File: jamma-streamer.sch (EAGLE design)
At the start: 64 parts, among them IC1 LM7805, J1 Audio line out, J2 ICSP, J4 DM3AT-SF-PEJM5, J5 KMMX-BSMT35S-B30TR, T1 TY-145P, T2 TY-145P, U1 CD74HC165MD16-M, U10 LM358DTD8-M, U2 ATMEGA328PB-AUR, U3 74HC4050D, U4 TLV757X / LP298X, U5 CD74HC165MD16-M, U6 CD74HC165MD16-M, U7 FT232RL, U8 DS3231SNT&R21-0042B_16-M, U9 NDT2955SOT-223-M, Y1 16MHz

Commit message: Reorg eagle libraries
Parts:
- B1: device S8411R:S8411-45R -> nma-eagle:S8411-45R
- C1, C2: device CMS:KEMET-C1206C334M5RAC -> nma-eagle:KEMET-C1206C334M5RAC
- C10, C4, C8: device CMS:KEMET-C1210C106K8N -> nma-eagle:KEMET-C1210C106K8N
- C11, C12, C13, C14, C3, C6, C7, C9: device CMS:KEMET-C1210C104K4J -> nma-eagle:KEMET-C1210C104K4J
- C5: device CMS:KEMET-C1206X334K5R -> nma-eagle:KEMET-C1206X334K5R
- D1, D2, D3-RX, D4-TX: device CMS:604-APTD1608LCGCK -> nma-eagle:604-APTD1608LCGCK
- D5: device RRE07VTM4SFHTR:RRE07VTM4SFHTR -> nma-eagle:RRE07VTM4SFHTR
- F1: device 1206L050YR:1206L050YRSMD -> nma-eagle:1206L050YRSMD
- J1: device SJ1-3523N:SJ1-3523N -> nma-eagle:SJ1-3523N
- J4: device DM3AT-SF-PEJM5:DM3AT-SF-PEJM5 -> nma-eagle:DM3AT-SF-PEJM5
- J5: device KMMX-BSMT35S-B30TR:KMMX-BSMT35S-B30TR -> nma-eagle:KMMX-BSMT35S-B30TR
- JAMMA_IN: device jamma_female_56:JAMMA_FEMALE_56 -> nma-eagle:JAMMA_FEMALE_56
- JAMMA_OUT_BTM: device JAMMA:JAMMA_BOTTOM -> nma-eagle:JAMMA_BOTTOM
- JAMMA_OUT_TOP: device JAMMA:JAMMA_TOP -> nma-eagle:JAMMA_TOP
- R1, R3, R4, R5: device CMS:BOURNS-652CHP0603FX1001ELF -> nma-eagle:BOURNS-652CHP0603FX1001ELF
- R10, R11, R12, R13: device nma-mouser:TE3550 -> nma-eagle:TE3550
- R14, R15, R16: device nma-mouser:ERJ-14NF2200U -> nma-eagle:ERJ-14NF2200U
- R2, R6, R7, R8, R9: device CMS:BOURNS-CRM2512AJW103ELF -> nma-eagle:BOURNS-CRM2512AJW103ELF
- S1: device 1825910-7:1825910-7 -> nma-eagle:1825910-7
- S2: device SamacSys_Parts:SS22SDP2 -> nma-eagle:SS22SDP2
- SYNC_POT: device SparkFun-Retired:TRIMPOTPTH -> nma-eagle:TRIMPOTPTH
- T1, T2: device TRIAD-TY-145P:TRIAD-TY-145P -> nma-eagle:TRIAD-TY-145P
- U1, U5, U6: device CD74HC165M:CD74HC165MD16-M -> nma-eagle:CD74HC165MD16-M
- U10: device LM358D:LM358DTD8-M -> nma-eagle:LM358DTD8-M
- U2: device ATMEGA328PB-AUR:ATMEGA328PB-AUR -> nma-eagle:ATMEGA328PB-AUR
- U3: device 74HC4050D:74HC4050D -> nma-eagle:74HC4050D
- U4: device LP2981-33DBVR:LP2981-33DBVRDBV5-M -> nma-eagle:LP2981-33DBVRDBV5-M
- U8: device DS3231:DS3231SNT&R21-0042B_16-M -> nma-eagle:DS3231SNT&R21-0042B_16-M
- U9: device NDT2955:NDT2955SOT-223-M -> nma-eagle:NDT2955SOT-223-M
- VGA_OUT: device harting-D-Sub-15:HARTING-DSUB-15-FEMALE -> nma-eagle:HARTING-DSUB-15-FEMALE
- Y1: device SparkFun-Clocks:CRYSTAL-16MHZPTH-HC49US -> nma-eagle:CRYSTAL-16MHZPTH-HC49US

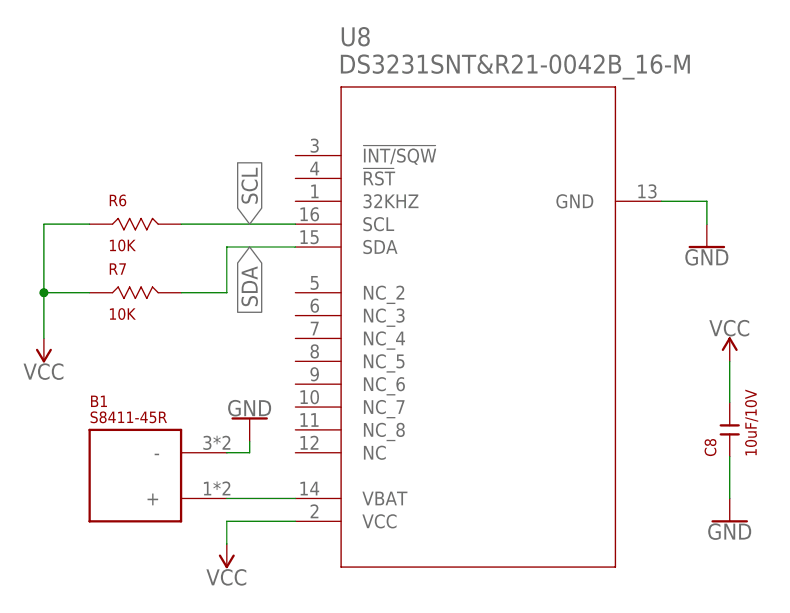
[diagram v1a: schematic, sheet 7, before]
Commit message: Changing battery holder to use CR2032
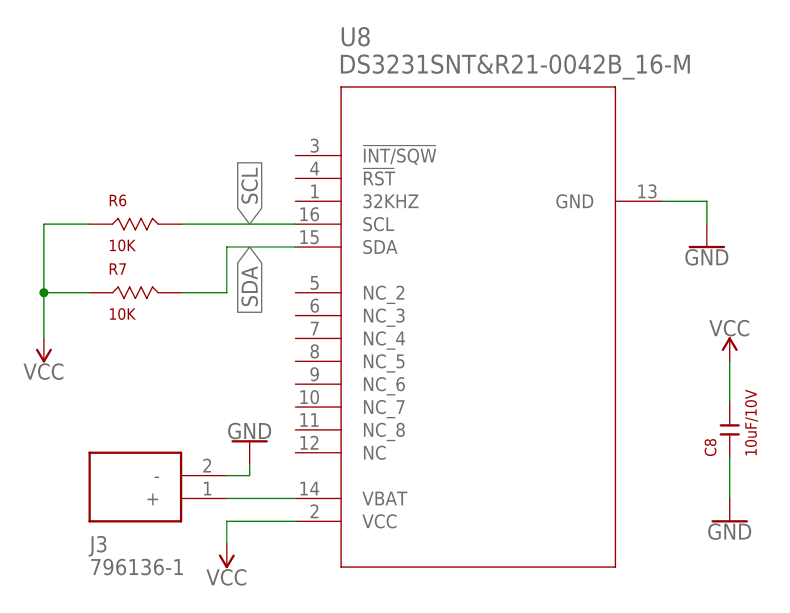
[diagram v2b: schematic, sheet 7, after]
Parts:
- removed B1: S8411-45R, nma-eagle:S8411-45R
- added J3: 796136-1, nma-eagle:796136-1
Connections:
- net GND: now also J3.-; no longer B1.-
- net N$31: now also J3.+; no longer B1.+
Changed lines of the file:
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@@
 <part name="SUPPLY19" library="SparkFun-PowerSymbols" library_urn="urn:adsk.eagle:library:530" deviceset="VCC" device=""/>
 <part name="GND29" library="SparkFun-PowerSymbols" library_urn="urn:adsk.eagle:library:530" deviceset="GND" device=""/>
-<part name="B1" library="nma-eagle" deviceset="S8411-45R" device=""/>
 <part name="C8" library="nma-eagle" deviceset="KEMET-C1210C106K8N" device="" value="10uF/10V"/>
 <part name="SUPPLY20" library="SparkFun-PowerSymbols" library_urn="urn:adsk.eagle:library:530" deviceset="VCC" device=""/>
@@
 <part name="R15" library="nma-eagle" deviceset="ERJ-14NF2200U" device="" value="220 ohms"/>
 <part name="R16" library="nma-eagle" deviceset="ERJ-14NF2200U" device="" value="220 ohms"/>
+<part name="J3" library="nma-eagle" deviceset="796136-1" device=""/>
 </parts>
 <sheets>
@@
 <attribute name="VALUE" x="38.1" y="48.006" size="1.778" layer="96" rot="R180" align="bottom-center"/>
 </instance>
-<instance part="GND29" gate="1" x="60.96" y="41.91" smashed="yes" rot="R180">
-<attribute name="VALUE" x="60.96" y="42.164" size="1.778" layer="96" rot="R180" align="top-center"/>
-</instance>
-<instance part="B1" gate="G$1" x="53.34" y="35.56" smashed="yes">
-<attribute name="NAME" x="43.18" y="43.18" size="1.27" layer="94"/>
-<attribute name="VALUE" x="43.18" y="41.402" size="1.27" layer="94"/>
+<instance part="GND29" gate="1" x="60.96" y="39.37" smashed="yes" rot="R180">
+<attribute name="VALUE" x="60.96" y="39.624" size="1.778" layer="96" rot="R180" align="top-center"/>
 </instance>
 <instance part="C8" gate="A" x="114.3" y="40.64" smashed="yes" rot="R90">
@@
 <instance part="GND30" gate="1" x="114.3" y="30.48" smashed="yes">
 <attribute name="VALUE" x="114.3" y="30.226" size="1.778" layer="96" align="top-center"/>
+</instance>
+<instance part="J3" gate="G$1" x="58.42" y="33.02" smashed="yes" rot="R180">
+<attribute name="NAME" x="43.18" y="27.94" size="1.778" layer="95" align="center-left"/>
+<attribute name="VALUE" x="43.18" y="25.4" size="1.778" layer="96" align="center-left"/>
 </instance>
 </instances>
@@
 <segment>
 <pinref part="GND29" gate="1" pin="GND"/>
-<wire x1="58.42" y1="38.1" x2="60.96" y2="38.1" width="0.1524" layer="91"/>
-<wire x1="60.96" y1="38.1" x2="60.96" y2="39.37" width="0.1524" layer="91"/>
-<pinref part="B1" gate="G$1" pin="-"/>
+<wire x1="60.96" y1="35.56" x2="60.96" y2="36.83" width="0.1524" layer="91"/>
+<pinref part="J3" gate="G$1" pin="-"/>
+<wire x1="60.96" y1="35.56" x2="58.42" y2="35.56" width="0.1524" layer="91"/>
 </segment>
 <segment>
@@
 <pinref part="U8" gate="A" pin="VBAT"/>
 <wire x1="58.42" y1="33.02" x2="66.04" y2="33.02" width="0.1524" layer="91"/>
-<pinref part="B1" gate="G$1" pin="+"/>
-</segment>
-</net>
+<pinref part="J3" gate="G$1" pin="+"/>
+</segment>
+</net>

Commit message: Added RTC with milliseconds accuracy
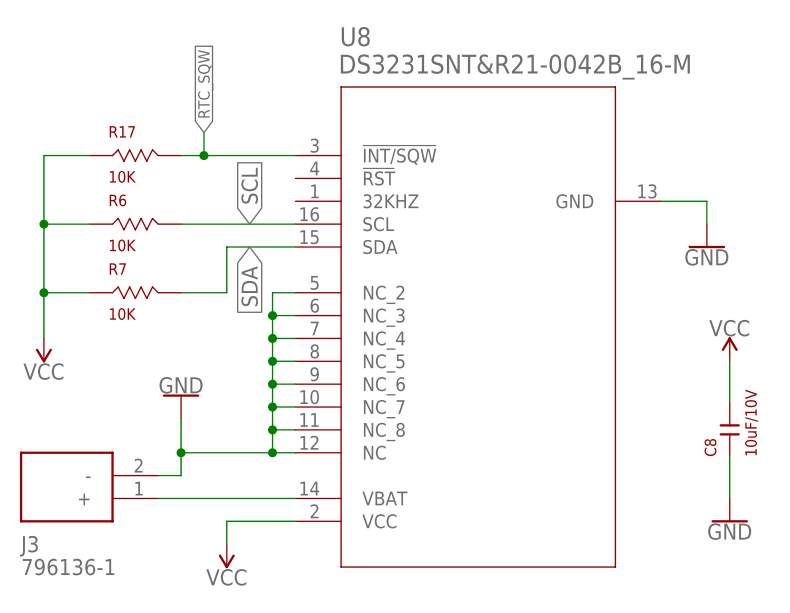
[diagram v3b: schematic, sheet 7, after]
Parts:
- added R17: 10K, nma-eagle:BOURNS-CRM2512AJW103ELF
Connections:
- new net RTC_SQW: R17.P$2, U2.PC3, U8.!INT/SQW
- net GND: now also U8.NC, U8.NC_2, U8.NC_3, U8.NC_4, U8.NC_5, U8.NC_6, U8.NC_7, U8.NC_8
- net VCC: now also R17.P$1
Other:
- moved on the sheet: J3
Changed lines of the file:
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@@
 <part name="R16" library="nma-eagle" deviceset="ERJ-14NF2200U" device="" value="220 ohms"/>
 <part name="J3" library="nma-eagle" deviceset="796136-1" device=""/>
+<part name="R17" library="nma-eagle" deviceset="BOURNS-CRM2512AJW103ELF" device="" value="10K"/>
 </parts>
 <sheets>
@@
 </segment>
 </net>
+<net name="RTC_SQW" class="0">
+<segment>
+<pinref part="U2" gate="G$1" pin="PC3"/>
+<wire x1="55.88" y1="63.5" x2="50.8" y2="63.5" width="0.1524" layer="91"/>
+<label x="50.8" y="63.5" size="1.27" layer="95" rot="R180" xref="yes"/>
+</segment>
+</net>
 </nets>
 </sheet>
@@
 <attribute name="VALUE" x="38.1" y="48.006" size="1.778" layer="96" rot="R180" align="bottom-center"/>
 </instance>
-<instance part="GND29" gate="1" x="60.96" y="39.37" smashed="yes" rot="R180">
-<attribute name="VALUE" x="60.96" y="39.624" size="1.778" layer="96" rot="R180" align="top-center"/>
+<instance part="GND29" gate="1" x="53.34" y="44.45" smashed="yes" rot="R180">
+<attribute name="VALUE" x="53.34" y="44.704" size="1.778" layer="96" rot="R180" align="top-center"/>
 </instance>
 <instance part="C8" gate="A" x="114.3" y="40.64" smashed="yes" rot="R90">
@@
 <attribute name="VALUE" x="114.3" y="30.226" size="1.778" layer="96" align="top-center"/>
 </instance>
-<instance part="J3" gate="G$1" x="58.42" y="33.02" smashed="yes" rot="R180">
-<attribute name="NAME" x="43.18" y="27.94" size="1.778" layer="95" align="center-left"/>
-<attribute name="VALUE" x="43.18" y="25.4" size="1.778" layer="96" align="center-left"/>
+<instance part="J3" gate="G$1" x="50.8" y="33.02" smashed="yes" rot="R180">
+<attribute name="NAME" x="35.56" y="27.94" size="1.778" layer="95" align="center-left"/>
+<attribute name="VALUE" x="35.56" y="25.4" size="1.778" layer="96" align="center-left"/>
+</instance>
+<instance part="R17" gate="A" x="48.26" y="71.12" smashed="yes">
+<attribute name="NAME" x="45.26" y="73.12" size="1.27" layer="94"/>
+<attribute name="VALUE" x="45.26" y="68.12" size="1.27" layer="94"/>
 </instance>
 </instances>
@@
 <junction x="38.1" y="55.88"/>
 <pinref part="SUPPLY19" gate="G$1" pin="VCC"/>
+<pinref part="R17" gate="A" pin="P$1"/>
+<wire x1="43.18" y1="71.12" x2="38.1" y2="71.12" width="0.1524" layer="91"/>
+<wire x1="38.1" y1="71.12" x2="38.1" y2="63.5" width="0.1524" layer="91"/>
+<junction x="38.1" y="63.5"/>
 </segment>
 <segment>
@@
 <segment>
 <pinref part="GND29" gate="1" pin="GND"/>
-<wire x1="60.96" y1="35.56" x2="60.96" y2="36.83" width="0.1524" layer="91"/>
+<wire x1="53.34" y1="35.56" x2="53.34" y2="38.1" width="0.1524" layer="91"/>
 <pinref part="J3" gate="G$1" pin="-"/>
-<wire x1="60.96" y1="35.56" x2="58.42" y2="35.56" width="0.1524" layer="91"/>
+<wire x1="53.34" y1="38.1" x2="53.34" y2="41.91" width="0.1524" layer="91"/>
+<wire x1="53.34" y1="35.56" x2="50.8" y2="35.56" width="0.1524" layer="91"/>
+<pinref part="U8" gate="A" pin="NC_2"/>
+<wire x1="66.04" y1="55.88" x2="63.5" y2="55.88" width="0.1524" layer="91"/>
+<wire x1="63.5" y1="55.88" x2="63.5" y2="53.34" width="0.1524" layer="91"/>
+<wire x1="63.5" y1="53.34" x2="63.5" y2="50.8" width="0.1524" layer="91"/>
+<wire x1="63.5" y1="50.8" x2="63.5" y2="48.26" width="0.1524" layer="91"/>
+<wire x1="63.5" y1="48.26" x2="63.5" y2="45.72" width="0.1524" layer="91"/>
+<wire x1="63.5" y1="45.72" x2="63.5" y2="43.18" width="0.1524" layer="91"/>
+<wire x1="63.5" y1="43.18" x2="63.5" y2="40.64" width="0.1524" layer="91"/>
+<wire x1="63.5" y1="40.64" x2="63.5" y2="38.1" width="0.1524" layer="91"/>
+<wire x1="63.5" y1="38.1" x2="53.34" y2="38.1" width="0.1524" layer="91"/>
+<junction x="53.34" y="38.1"/>
+<pinref part="U8" gate="A" pin="NC"/>
+<wire x1="66.04" y1="38.1" x2="63.5" y2="38.1" width="0.1524" layer="91"/>
+<junction x="63.5" y="38.1"/>
+<pinref part="U8" gate="A" pin="NC_8"/>
+<wire x1="66.04" y1="40.64" x2="63.5" y2="40.64" width="0.1524" layer="91"/>
+<junction x="63.5" y="40.64"/>
+<pinref part="U8" gate="A" pin="NC_7"/>
+<wire x1="66.04" y1="43.18" x2="63.5" y2="43.18" width="0.1524" layer="91"/>
+<junction x="63.5" y="43.18"/>
+<pinref part="U8" gate="A" pin="NC_6"/>
+<wire x1="66.04" y1="45.72" x2="63.5" y2="45.72" width="0.1524" layer="91"/>
+<junction x="63.5" y="45.72"/>
+<pinref part="U8" gate="A" pin="NC_5"/>
+<wire x1="66.04" y1="48.26" x2="63.5" y2="48.26" width="0.1524" layer="91"/>
+<junction x="63.5" y="48.26"/>
+<pinref part="U8" gate="A" pin="NC_4"/>
+<wire x1="66.04" y1="50.8" x2="63.5" y2="50.8" width="0.1524" layer="91"/>
+<junction x="63.5" y="50.8"/>
+<pinref part="U8" gate="A" pin="NC_3"/>
+<wire x1="66.04" y1="53.34" x2="63.5" y2="53.34" width="0.1524" layer="91"/>
+<junction x="63.5" y="53.34"/>
 </segment>
 <segment>
@@
 <segment>
 <pinref part="U8" gate="A" pin="VBAT"/>
-<wire x1="58.42" y1="33.02" x2="66.04" y2="33.02" width="0.1524" layer="91"/>
+<wire x1="50.8" y1="33.02" x2="66.04" y2="33.02" width="0.1524" layer="91"/>
 <pinref part="J3" gate="G$1" pin="+"/>
 </segment>
 </net>
+<net name="RTC_SQW" class="0">
+<segment>
+<pinref part="R17" gate="A" pin="P$2"/>
+<wire x1="55.88" y1="71.12" x2="53.34" y2="71.12" width="0.1524" layer="91"/>
+<wire x1="55.88" y1="71.12" x2="55.88" y2="73.66" width="0.1524" layer="91"/>
+<junction x="55.88" y="71.12"/>
+<label x="55.88" y="73.66" size="1.27" layer="95" rot="R90" xref="yes"/>
+<pinref part="U8" gate="A" pin="!INT/SQW"/>
+<wire x1="66.04" y1="71.12" x2="55.88" y2="71.12" width="0.1524" layer="91"/>
+</segment>
+</net>

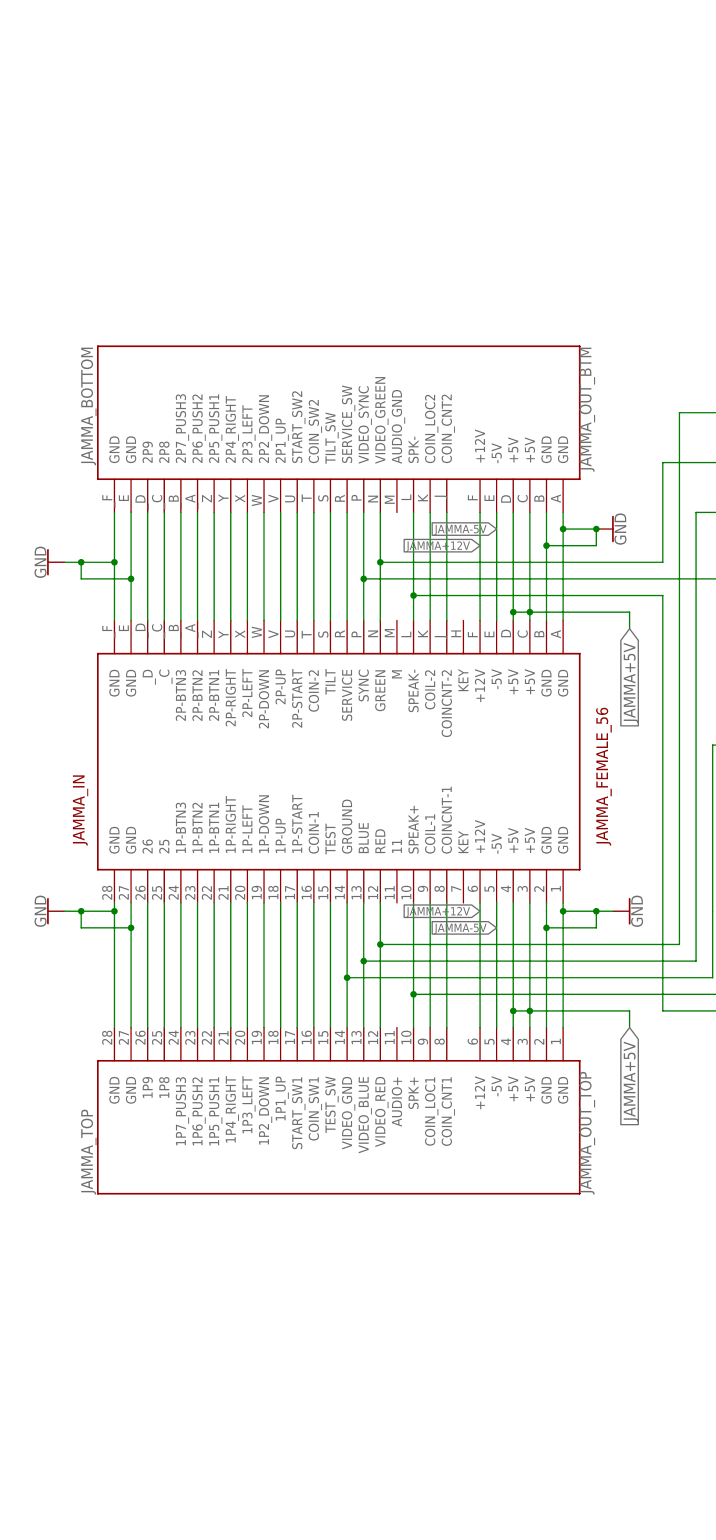
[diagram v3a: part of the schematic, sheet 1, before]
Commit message: Finalization + add jamma connector horiz
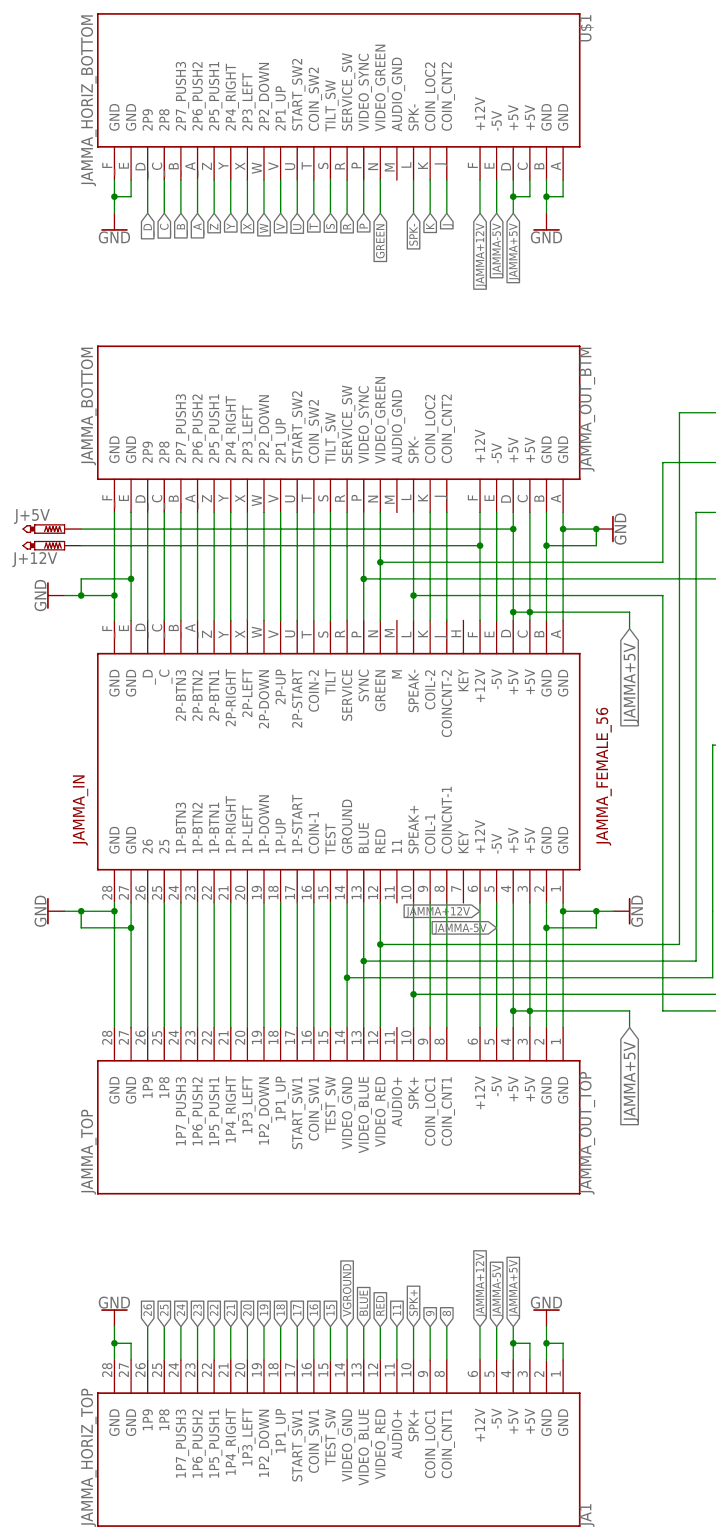
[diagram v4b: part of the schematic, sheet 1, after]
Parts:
- removed J5: KMMX-BSMT35S-B30TR, nma-eagle:KMMX-BSMT35S-B30TR
- added +3.3V, +5V, GND, J+12V, J+5V, USBVCC: PTR1TP15SQ, testpad:PTR1TP15SQ
- added J6: 292304-1, nma-eagle:292304-1
- added JA1: JAMMA_HORIZ_TOP, nma-eagle:JAMMA_HORIZ_TOP
- added U$1: JAMMA_HORIZ_BOTTOM, nma-eagle:JAMMA_HORIZ_BOTTOM
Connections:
- new net 11: JA1.AUDIO+
- net 15: now also JA1.TEST_SW
- net 16: now also JA1.COIN_SW1
- net 17: now also JA1.START_SW1
- net 18: now also JA1.1P1_UP
- net 19: now also JA1.1P2_DOWN
- net 20: now also JA1.1P3_LEFT
- net 21: now also JA1.1P4_RIGHT
- net 22: now also JA1.1P5_PUSH1
- net 23: now also JA1.1P6_PUSH2
- net 24: now also JA1.1P7_PUSH3
- net 25: now also JA1.1P8
- net 26: now also JA1.1P9
- net 8: now also JA1.COIN_CNT1
- net 9: now also JA1.COIN_LOC1
- net BLUE: now also JA1.VIDEO_BLUE
- net D+: now also J6.D+; no longer J5.3
- net D-: now also J6.D-; no longer J5.2
- net GND: now also GND.TP, J6.GND, JA1.GND@1, JA1.GND@2, JA1.GND@3, JA1.GND@4, U$1.GND@1, U$1.GND@2, U$1.GND@3, U$1.GND@4; no longer J5.5, J5.MH1, J5.MH2, J5.MH3, J5.MH4
- net GREEN: now also U$1.VIDEO_GREEN
- net J: now also U$1.COIN_CNT2
- net JAMMA+12V: now also J+12V.TP, JA1.+12V, U$1.+12V
- net JAMMA+5V: now also J+5V.TP, JA1.+5V@1, JA1.+5V@2, U$1.+5V@1, U$1.+5V@2
- net JAMMA-5V: now also JA1.-5V, U$1.-5V
- net K: now also U$1.COIN_LOC2
- net P: now also U$1.VIDEO_SYNC
- net R: now also U$1.SERVICE_SW
- net RED: now also JA1.VIDEO_RED
- net S: now also U$1.TILT_SW
- net SPK+: now also JA1.SPK+
- net SPK-: now also U$1.SPK-
- net T: now also U$1.COIN_SW2
- net U: now also U$1.START_SW2
- net USBVCC: now also USBVCC.TP
- net USB_V: now also J6.VBUS; no longer J5.1
- net V: now also U$1.2P1_UP
- net VCC: now also +5V.TP
- net VCC_2: now also +3.3V.TP
- net VGROUND: now also JA1.VIDEO_GND
- net W: now also U$1.2P2_DOWN
- net X: now also U$1.2P3_LEFT
- net Y: now also U$1.2P4_RIGHT
- net Z: now also U$1.2P5_PUSH1
- net _A: now also U$1.2P6_PUSH2
- net _B: now also U$1.2P7_PUSH3
- net _C: now also U$1.2P8
- net _D: now also U$1.2P9
